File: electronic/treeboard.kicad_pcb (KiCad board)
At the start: 4 copper layers, 85 x 135.6 mm, 101 parts, among them J12 Conn_02x10_Counter_Clockwise, J2 Conn_01x06_MountingPin, J3 Conn_01x06_MountingPin, J4 USB_C_Receptacle_USB2.0, J5 Conn_01x06_Socket, J6 Conn_01x06_Socket, J7 Conn_01x06_Socket, J8 Conn_02x10_Counter_Clockwise, J9 Conn_02x05_Odd_Even, SW1 SW_Push_45deg, SW10 SW_Push_45deg, SW11 SW_Push_45deg, SW12 SW_Push_45deg, SW13 SW_Push_45deg, SW14 SW_Push_45deg, SW15 SW_Push_45deg, SW16 SW_Push_45deg, SW17 SW_Push_45deg, SW18 SW_Push_45deg, SW19 SW_Push_45deg, SW2 SW_Push_45deg, SW20 RotaryEncoder, SW3 SW_Push_45deg, SW4 SW_Push_45deg, SW5 SW_Push_45deg, SW6 SW_Push_45deg, SW7 SW_Push_45deg, SW8 SW_Push_45deg, SW9 SW_Push_45deg, U1 TXB0104RUT, U6 BMD-340-A-R, U7 TXB0104RUT, Y2 32.064kHz

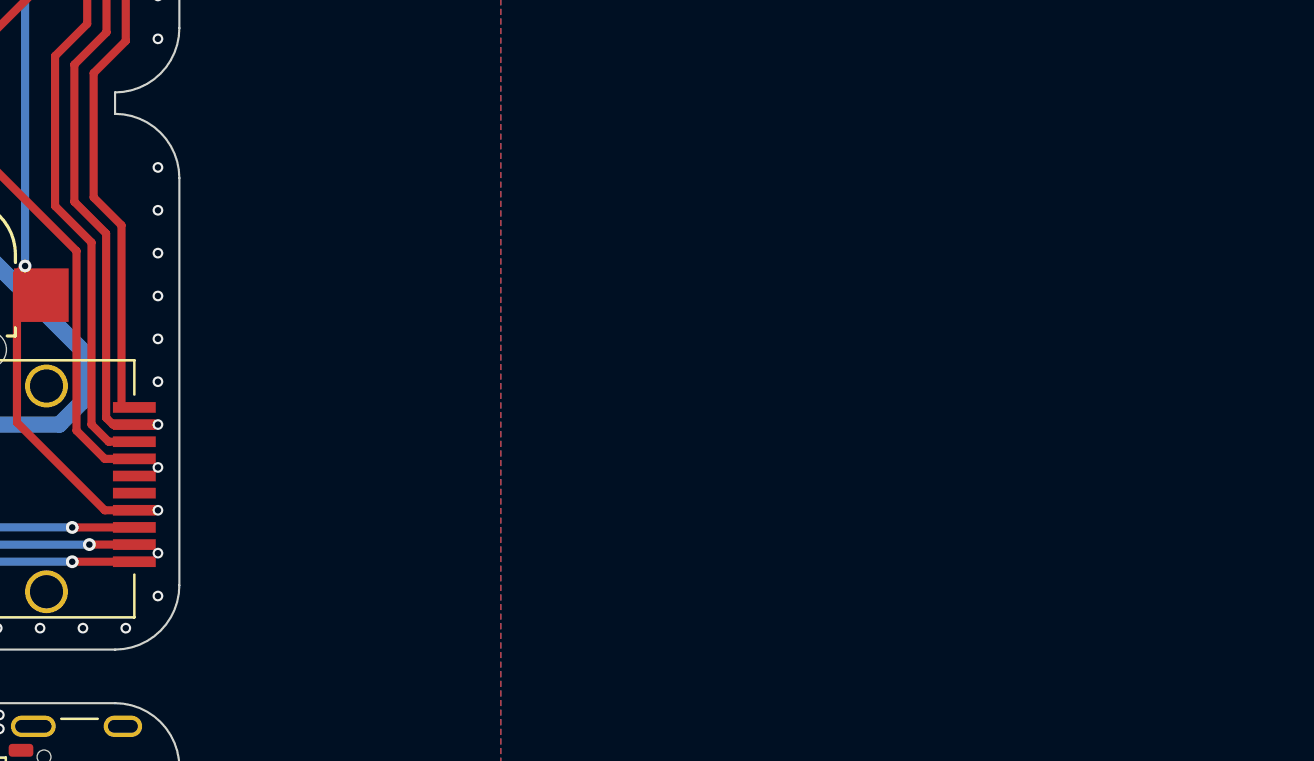
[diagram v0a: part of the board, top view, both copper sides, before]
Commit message: backup before switch
switching to nrf52840 feather
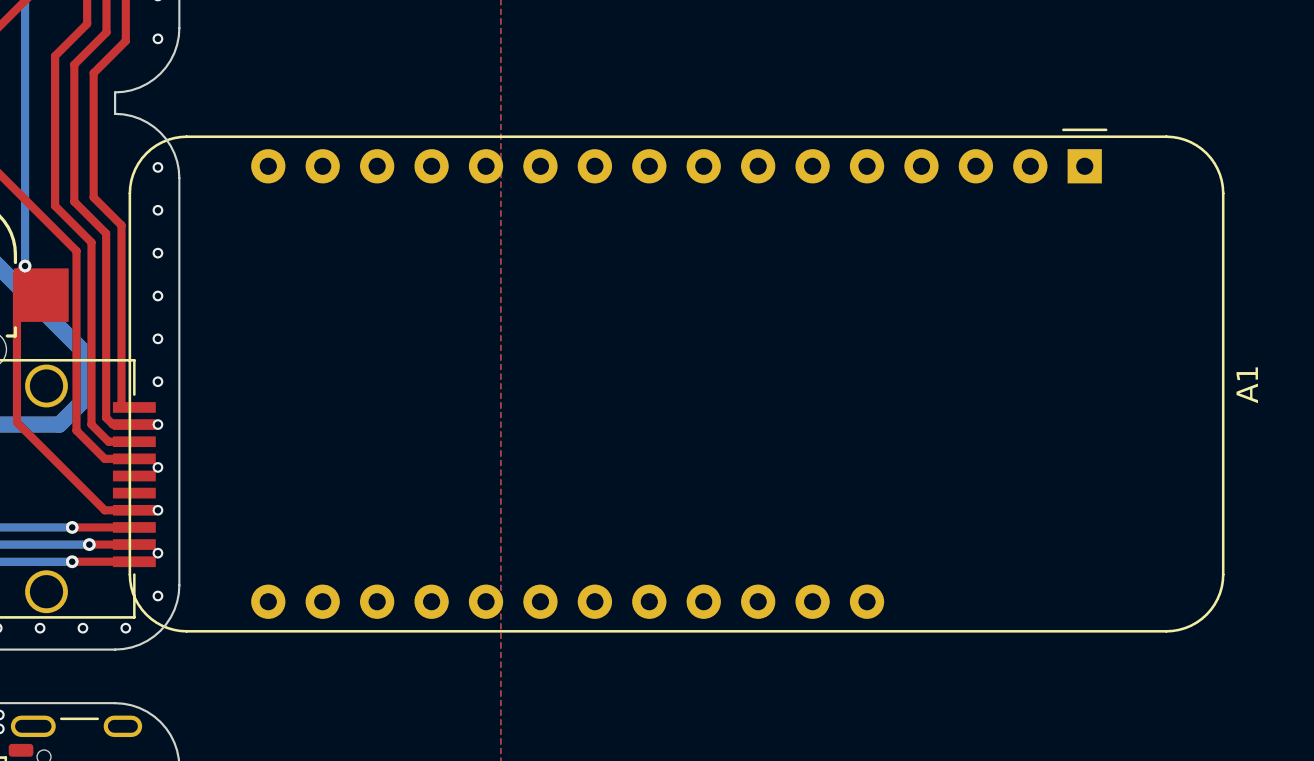
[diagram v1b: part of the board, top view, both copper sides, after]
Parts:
- added A1: Adafruit_Feather_Generic, Module:Adafruit_Feather, F.Cu at (127.2, 62.4)
- L1: value 15n -> 1u
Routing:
- net unconnected-(A1-MOSI-Pad12): vias 0 -> 2
- net (no net): vias 95 -> 93
